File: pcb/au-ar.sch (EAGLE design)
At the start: 79 parts, among them U1 TPD12S520DBTR, U2 TPD12S521DBTR

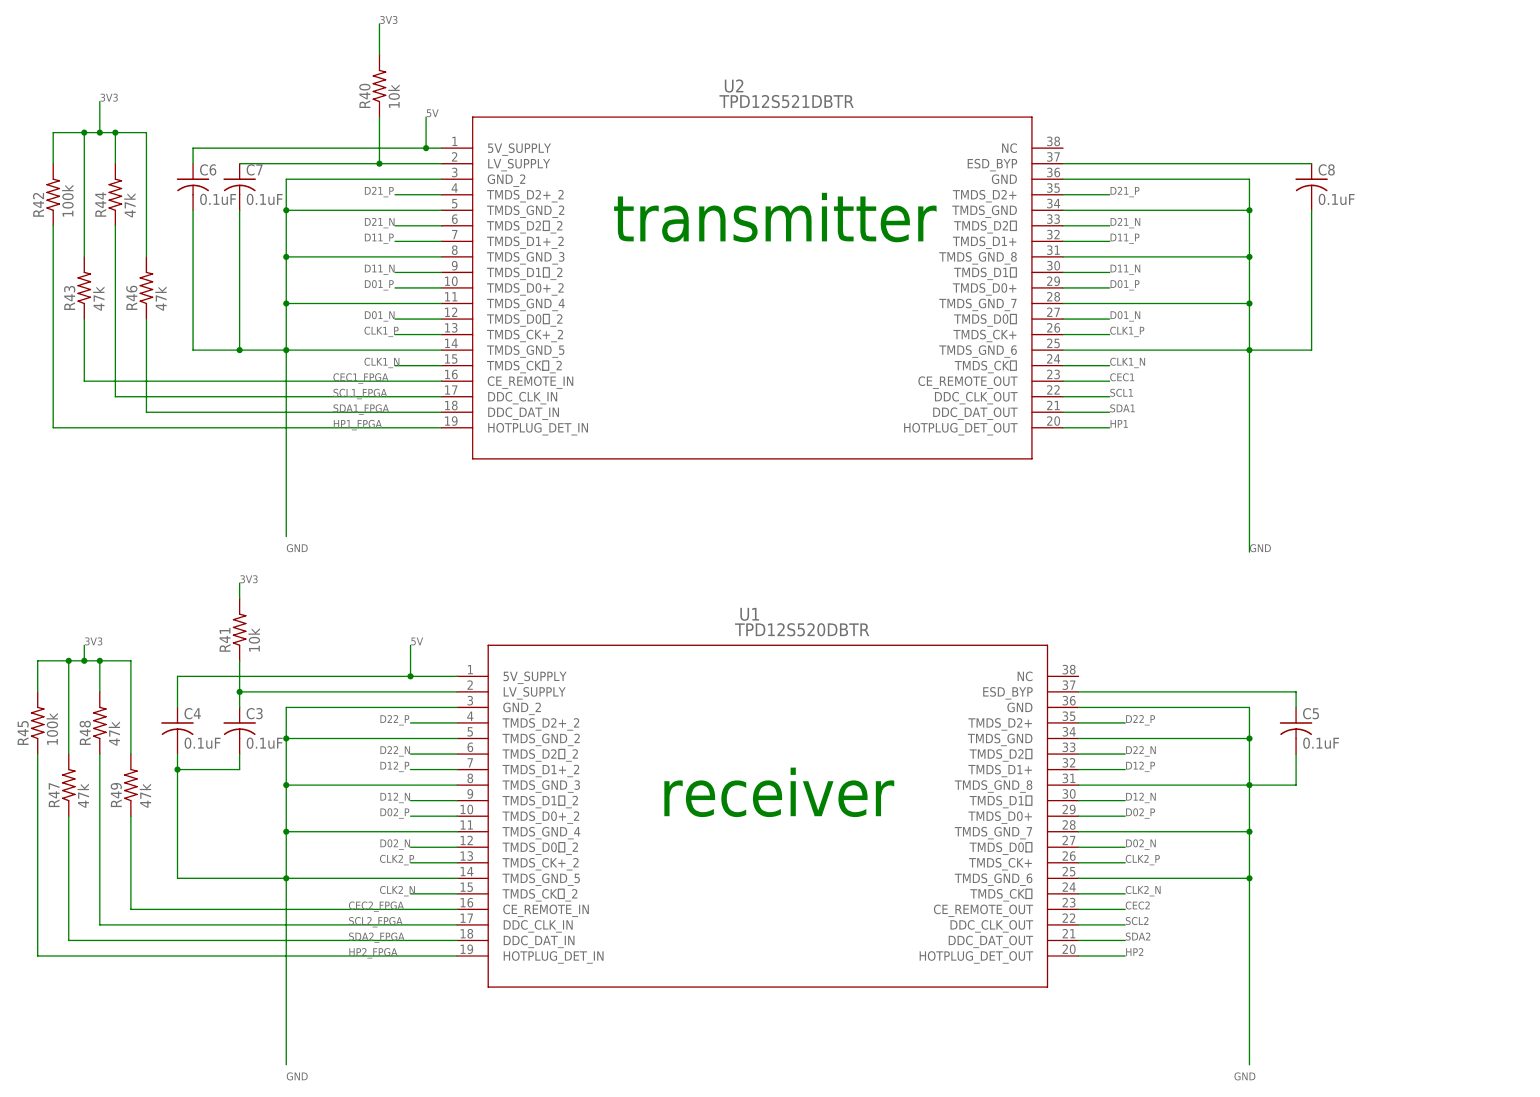
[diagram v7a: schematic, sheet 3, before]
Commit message: started rerouting with new esd protection chips
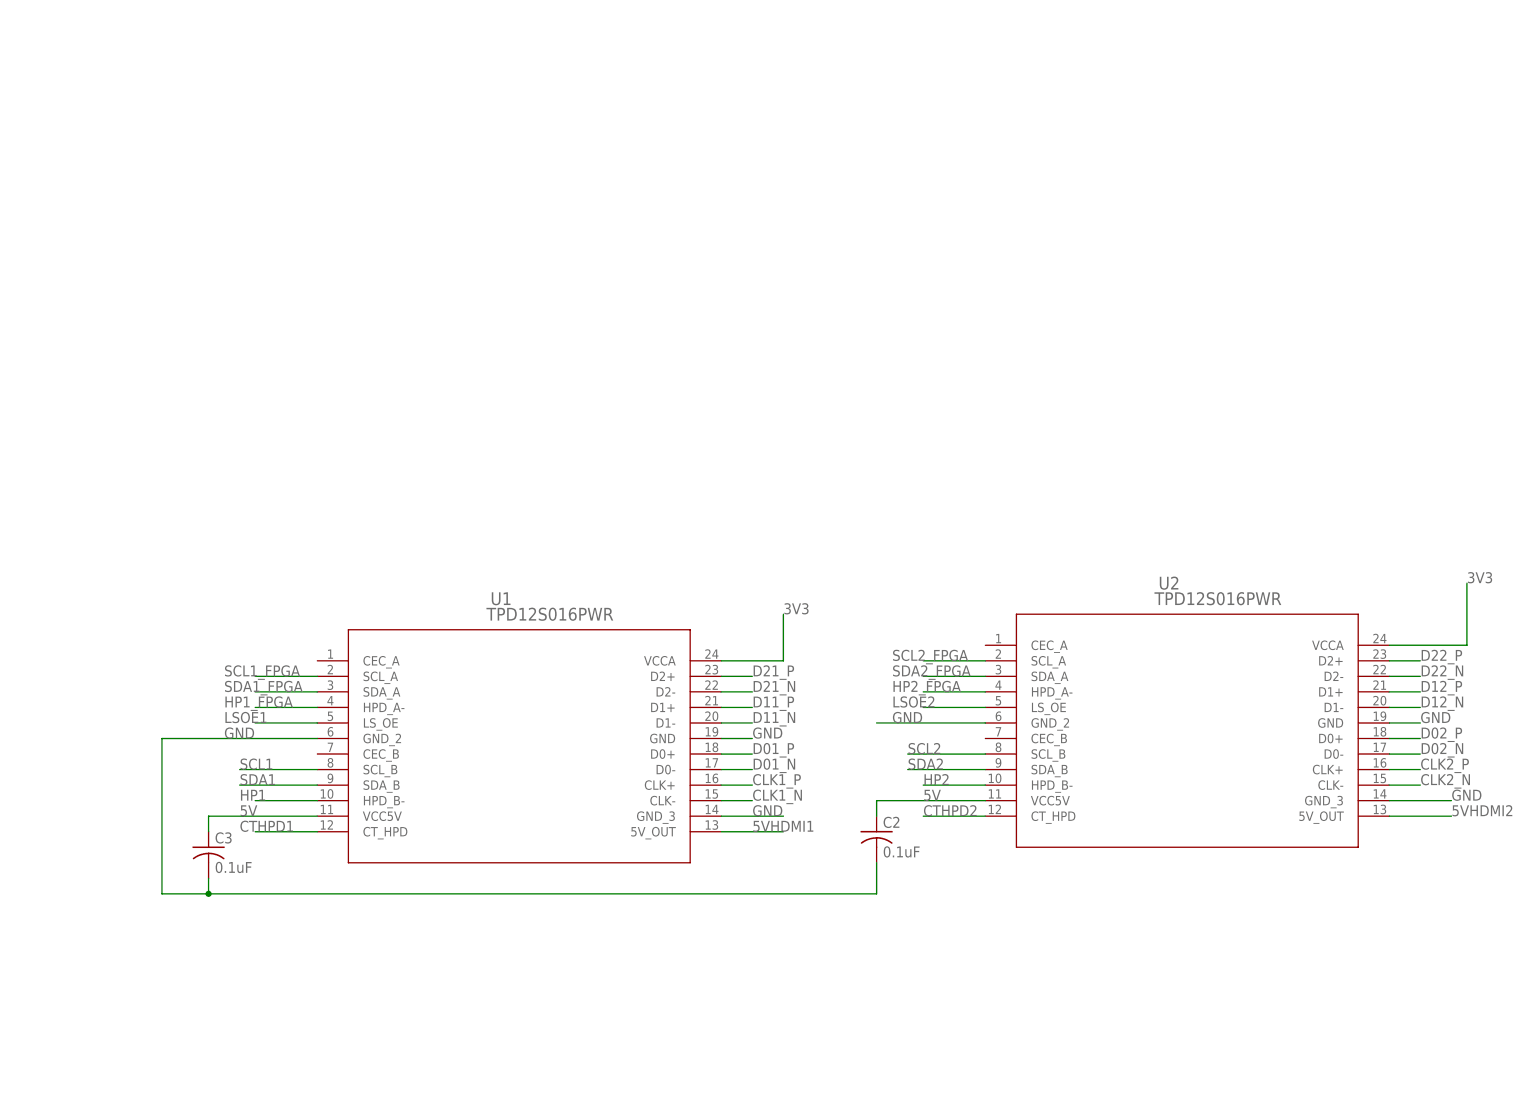
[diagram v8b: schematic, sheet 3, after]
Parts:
- removed C4, C5, C6, C7, C8: 0.1uF, rcl:C-USC0603
- removed R28, R37: 1k, rcl:R-US_R0603
- removed R31, R32, R33, R34, R43, R44, R46, R47, R48, R49: 47k, rcl:R-US_R0603
- removed R35: NP, rcl:R-US_R0603
- removed R36, R40, R41: 10k, rcl:R-US_R0603
- removed R38, R39: 27k, rcl:R-US_R0603
- removed R42, R45: 100k, rcl:R-US_R0603
- added C2: 0.1uF, rcl:C-USC0603
- U1: value TPD12S520DBTR -> TPD12S016PWR; device TDP12S520:TPD12S520DBTR -> lupa300-components:TPD12S016PWR
- U2: value TPD12S521DBTR -> TPD12S016PWR; device TDP12S521:TPD12S521DBTR -> lupa300-components:TPD12S016PWR
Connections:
- removed net CEC1: HDMI_1.13, R39.2, U2.CE_REMOTE_OUT
- removed net CEC1_FPGA: B1C.37, R43.1, U2.CE_REMOTE_IN
- removed net CEC2: HDMI_2.13, R38.2, U1.CE_REMOTE_OUT
- removed net CEC2_FPGA: B1A.39, R49.1, U1.CE_REMOTE_IN
- removed net N$1: C5.1, U1.ESD_BYP
- removed net N$11: HDMI_1.14, R36.2
- removed net N$12: C3.1, R41.1, U1.LV_SUPPLY
- removed net N$15: C7.1, R40.1, U2.LV_SUPPLY
- removed net N$16: C8.1, U2.ESD_BYP
- removed net N$2: HDMI_2.14, R35.2
- new net CTHPD1: U1.CT_HPD
- new net CTHPD2: U2.CT_HPD
- new net LSOE1: B1C.37, U1.LS_OE
- new net LSOE2: B1A.39, U2.LS_OE
- net 3V3: now also U1.VCCA, U2.VCCA; no longer R38.1, R39.1, R40.2, R41.2, R42.2, R43.2, R44.2, R45.2, R46.2, R47.2, R48.2, R49.2
- net 5V: now also C2.1, C3.1, U1.VCC5V, U2.VCC5V; no longer C4.1, C6.1, R31.1, R32.1, R33.1, R34.1, U1.5V_SUPPLY, U2.5V_SUPPLY
- net 5VHDMI1: now also U1.5V_OUT; no longer R37.1
- net 5VHDMI2: now also U2.5V_OUT; no longer R28.1
- net CLK1_N: now also U1.CLK-; no longer U2.TMDS_CK, U2.TMDS_CK_2
- net CLK1_P: now also U1.CLK+; no longer U2.TMDS_CK+, U2.TMDS_CK+_2
- net CLK2_N: now also U2.CLK-; no longer U1.TMDS_CK, U1.TMDS_CK_2
- net CLK2_P: now also U2.CLK+; no longer U1.TMDS_CK+, U1.TMDS_CK+_2
- net D01_N: now also U1.D0-; no longer U2.TMDS_D0, U2.TMDS_D0_2
- net D01_P: now also U1.D0+; no longer U2.TMDS_D0+, U2.TMDS_D0+_2
- net D02_N: now also U2.D0-; no longer U1.TMDS_D0, U1.TMDS_D0_2
- net D02_P: now also U2.D0+; no longer U1.TMDS_D0+, U1.TMDS_D0+_2
- net D11_N: now also U1.D1-; no longer U2.TMDS_D1, U2.TMDS_D1_2
- net D11_P: now also U1.D1+; no longer U2.TMDS_D1+, U2.TMDS_D1+_2
- net D12_N: now also U2.D1-; no longer U1.TMDS_D1, U1.TMDS_D1_2
- net D12_P: now also U2.D1+; no longer U1.TMDS_D1+, U1.TMDS_D1+_2
- net D21_N: now also U1.D2-; no longer U2.TMDS_D2, U2.TMDS_D2_2
- net D21_P: now also U1.D2+; no longer U2.TMDS_D2+, U2.TMDS_D2+_2
- net D22_N: now also U2.D2-; no longer U1.TMDS_D2, U1.TMDS_D2_2
- net D22_P: now also U2.D2+; no longer U1.TMDS_D2+, U1.TMDS_D2+_2
- net GND: now also C2.2, U1.GND_3, U2.GND_3; no longer C4.2, C5.2, C6.2, C7.2, C8.2, R35.1, R36.1, U1.TMDS_GND, U1.TMDS_GND_2, U1.TMDS_GND_3, U1.TMDS_GND_4, U1.TMDS_GND_5, U1.TMDS_GND_6, U1.TMDS_GND_7, U1.TMDS_GND_8, U2.TMDS_GND, U2.TMDS_GND_2, U2.TMDS_GND_3, U2.TMDS_GND_4, U2.TMDS_GND_5, U2.TMDS_GND_6, U2.TMDS_GND_7, U2.TMDS_GND_8
- net HP1: now also U1.HPD_B-; no longer R37.2, U2.HOTPLUG_DET_OUT
- net HP1_FPGA: now also U1.HPD_A-; no longer R42.1, U2.HOTPLUG_DET_IN
- net HP2: now also U2.HPD_B-; no longer R28.2, U1.HOTPLUG_DET_OUT
- net HP2_FPGA: now also U2.HPD_A-; no longer R45.1, U1.HOTPLUG_DET_IN
- net SCL1: now also U1.SCL_B; no longer R33.2, U2.DDC_CLK_OUT
- net SCL1_FPGA: now also U1.SCL_A; no longer R44.1, U2.DDC_CLK_IN
- net SCL2: now also U2.SCL_B; no longer R31.2, U1.DDC_CLK_OUT
- net SCL2_FPGA: now also U2.SCL_A; no longer R48.1, U1.DDC_CLK_IN
- net SDA1: now also U1.SDA_B; no longer R34.2, U2.DDC_DAT_OUT
- net SDA1_FPGA: now also U1.SDA_A; no longer R46.1, U2.DDC_DAT_IN
- net SDA2: now also U2.SDA_B; no longer R32.2, U1.DDC_DAT_OUT
- net SDA2_FPGA: now also U2.SDA_A; no longer R47.1, U1.DDC_DAT_IN
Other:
- note removed: "receiver"
- note removed: "receiver input"
- note removed: "transmitter"
- note removed: "transmitter output"
- moved on the sheet: C3
